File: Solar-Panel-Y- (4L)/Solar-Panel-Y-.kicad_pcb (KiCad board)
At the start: 4 copper layers, 64 x 58 mm, 85 parts, among them J1 FTS-107-01-X-DV-A, J2 BM02B-SRSS-TB, Q1 BSS138DWQ-7, Q2 MBT2222ADW1T1, Q3 BSS138DWQ-7, Q4 MBT2222ADW1T1, SW1 D2F-L2-A1, SW2 D2F-L2-A, U1 BQ25570RGRR, U2 TSL2561

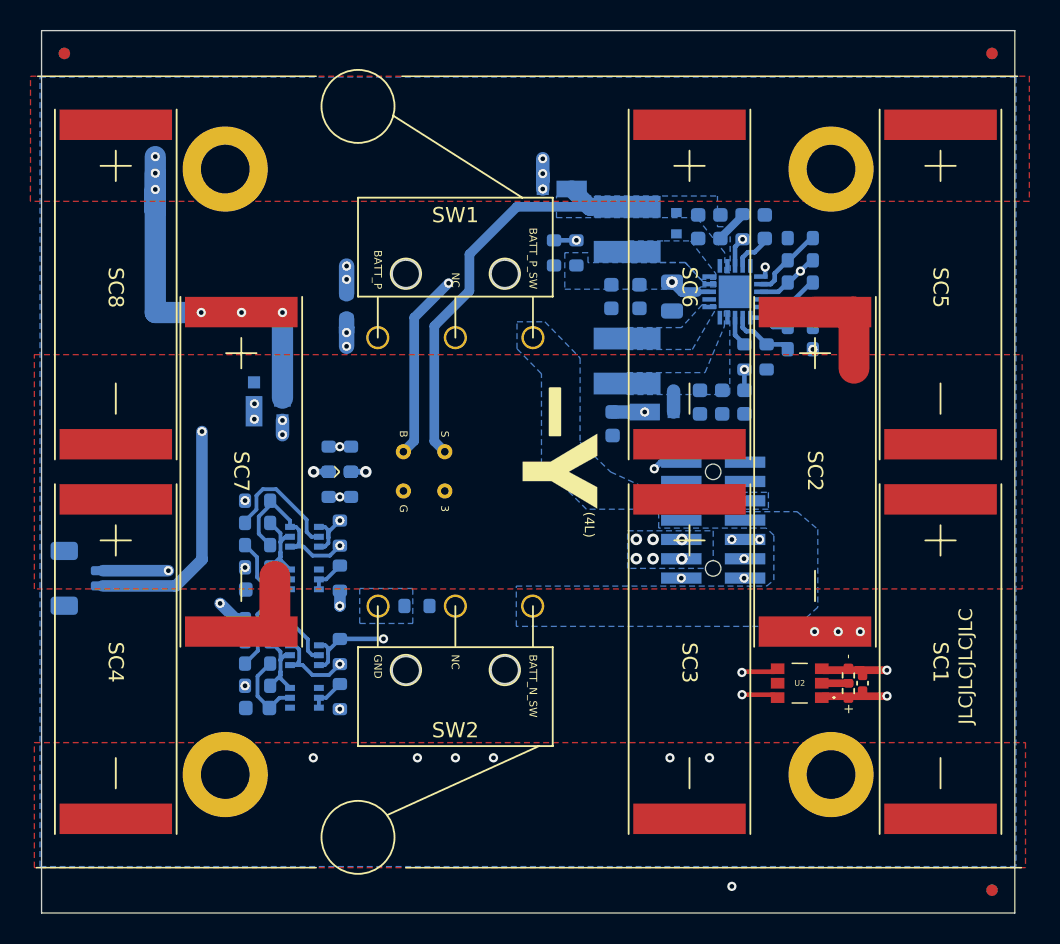
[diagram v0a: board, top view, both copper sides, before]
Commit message: Y- board changes for Rev B3/01
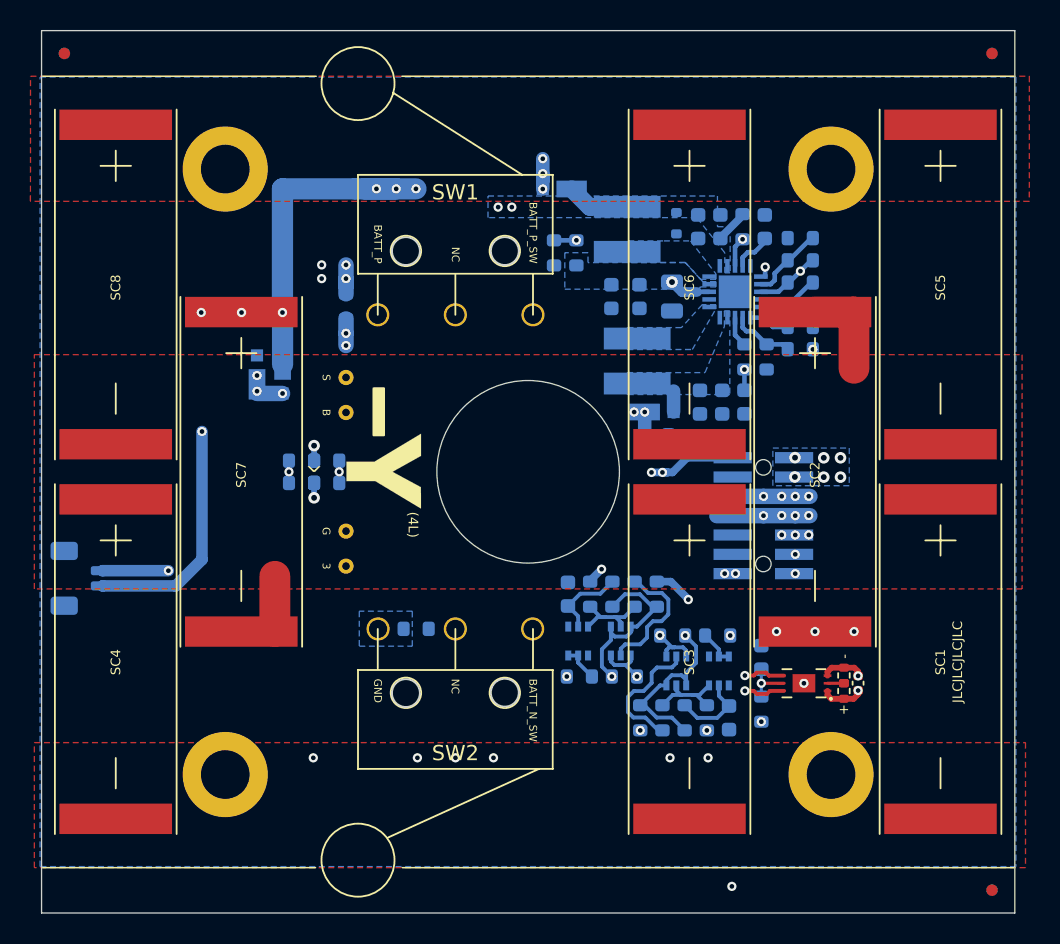
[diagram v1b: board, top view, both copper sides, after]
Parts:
- added C14: 1uF, Capacitor_SMD:C_0603_1608Metric, B.Cu at (120.3, 76.2)
- added R32: 1K, Resistor_SMD:R_0603_1608Metric, B.Cu at (120.3, 79.6)
- Q1, Q3: value BSS138DWQ-7 -> NX3008NBKS
- R1, R12, R13, R16, R17, R18, R2, R3, R31, R4: value 0 -> 0R
- R14, R15, R19, R20: value DNI -> DNI (0R)
- R21, R26: value 680 -> 680R
- U2: value TSL2561 -> BH1750FVI; footprint solarpanels:TSL2561 -> solarpanels:BH1750FVI
- moved C13 31.0 mm to (118.2, 80.2), turned to -90 degrees
- moved R28 29.6 mm to (116.7, 80.2), turned to 90 degrees
- moved R30 28.3 mm to (115.3, 80.2), turned to 90 degrees
- moved Q3 27.3 mm to (117.5, 77.1), turned to -90 degrees
- moved R26 27.1 mm to (113.8, 80.2), turned to 90 degrees
- moved R24 27.0 mm to (113.4, 72.0), turned to -90 degrees
- moved R29 26.0 mm to (112.3, 80.2), turned to 90 degrees
- moved R21 25.2 mm to (112.0, 72.0), turned to -90 degrees
- moved R27 25.2 mm to (117.4, 74.8), turned to 180 degrees
- moved Q4 24.5 mm to (114.7, 77.1), turned to -90 degrees
- moved R25 23.5 mm to (110.5, 72.0), turned to 90 degrees
- moved R23 21.9 mm to (109.0, 72.0), turned to -90 degrees
- moved R20 21.9 mm to (114.5, 74.8), turned to 180 degrees
- moved Q2 21.9 mm to (111.1, 75.1), turned to 90 degrees
- moved R19 20.9 mm to (111.3, 77.5), turned to 0 degrees
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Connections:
- J1 pad 1: unconnected-(J1-Pad1) -> BATT_P
- J1 pad 10: BATT_P -> GND
- J1 pad 12: BATT_P -> unconnected-(J1-Pin_12-Pad12)
- J1 pad 3: GND -> BATT_P
- J2 pad MP: (no net) -> GND
- U2 pad 4: SCL_LS -> SDA_LS
- U2 pad 5: unconnected-(U2-Pad5) -> Net-(U2-DVI)
- U2 pad 6: SDA_LS -> SCL_LS
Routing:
- net SCL_LS: track 49.6 -> 23.6 mm
- net SDA_LS: track 43.2 -> 20.4 mm
- net SDA: track 35.1 -> 16.4 mm
- net SCL: track 32.7 -> 19.6 mm
- net BATT_P_SW: track 41.6 -> 51.7 mm, vias 1 -> 5
- net VSOLAR: track 32.1 -> 24.5 mm, vias 0 -> 2
- net BATT_N_SW: track 30.6 -> 37.6 mm, vias 1 -> 5
- net COIL_N: track 26.6 -> 32.2 mm, vias 2 -> 3
- net COIL_P: track 32.4 -> 37.7 mm, vias 2 -> 3
- net /coil: track 7479.5 -> 7475.5 mm
- net Net-(U2-DVI): track 0.00 -> 3.30 mm, vias 0 -> 1
- net GND: track 4.56 -> 2.78 mm, vias 10 -> 11
- net /VSOLAR_FULL: track 30.6 -> 31.6 mm
- net +3V3: track 9.38 -> 8.62 mm, vias 10 -> 13
- net Net-(D3-K): track 10.8 -> 11.6 mm, vias 4 -> 3
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- added copper zone on In2.Cu, net BATT_N_SW
- added copper zone on In2.Cu, net BATT_P_SW
- removed copper zone on B.Cu, net BATT_N_SW
- removed copper zone on B.Cu, net BATT_P_SW
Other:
- outline, holes or cut-outs redrawn
- board text added: "1.BATT_P 3.BATT_P 5.BATT_P_SW 7.BATT_N_SW 9.3V3 11.SDA 13.SCL"
- board text added: "2.COIL_P 4.GND 6.BATT_P_SW 8.BATT_N_SW 10.GND 12.NC 14.COIL_N"
- board text added: "Rev B3/01"
- board text removed: "1.NC 3.GND 5.BATT_P_SW 7.BATT_N_SW 9.3V3 11.SDA 13.SCL"
- board text removed: "2.COIL_P 4.GND 6.BATT_P_SW 8.BATT_N_SW 10.BATT_P 12.BATT_P 14.COIL_N"
- board text removed: "Rev B2/01"

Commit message: Updated light sensor to OPT 3001, Updated solar diodes.
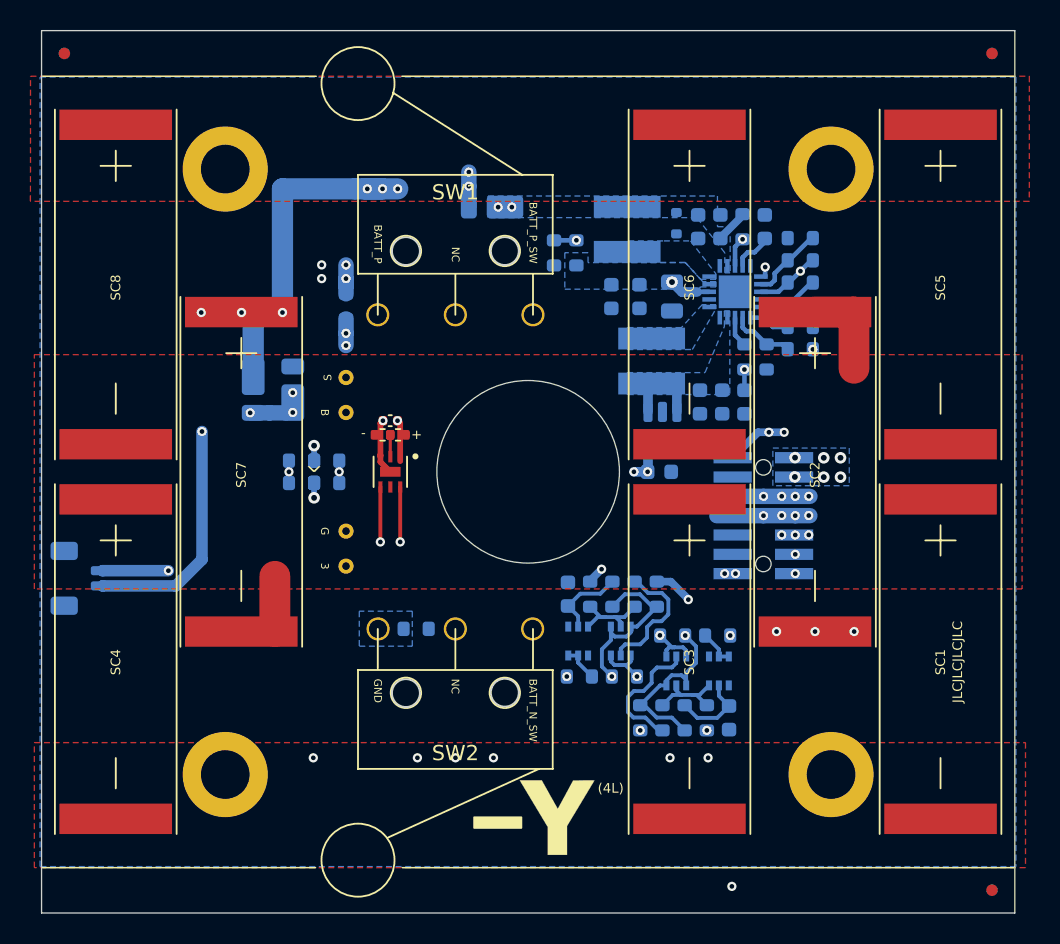
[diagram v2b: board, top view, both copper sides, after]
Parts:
- removed C14: 1uF, Capacitor_SMD:C_0603_1608Metric
- removed D5: MSS1P4-M3_89A, solarpanels:MICROSMP
- removed the R32 at (120.3, 79.6)
- added U3: MAX40200AUK, Package_TO_SOT_SMD:SOT-23-5, B.Cu at (113.8, 61.2)
- D2, D3, D4: value MSS1P4-M3_89A -> DFLS130L-7; footprint solarpanels:MICROSMP -> Diode_SMD:D_PowerDI-123
- U2: value BH1750FVI -> OPT3001; footprint solarpanels:BH1750FVI -> solarpanels:OPT3001
- moved C1 35.3 mm to (95.9, 60.6), turned to 0 degrees
- moved R2 34.2 mm to (95.4, 61.6), turned to 0 degrees
- moved R1 33.8 mm to (96.4, 61.6), turned to 0 degrees
- moved U2 30.5 mm to (95.9, 64.0), turned to -90 degrees
- moved Ref** 30.1 mm to (123.9, 87.7), turned to 0 degrees
- moved D2 17.2 mm to (102.6, 46.6), turned to 180 degrees
- moved D3 2.55 mm to (89.5, 58.6)
- moved C11 2.41 mm to (113.6, 64.0)
- moved D4 2.17 mm to (86.9, 58.6)
- moved L2 0.95 mm to (113.1, 56.7)
- renumbered R31 to R32, S to TP1, G to TP2, 3 to TP3, B to TP4
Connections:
- C10 pad 1: Net-(D2-A) -> Net-(U1-VOUT)
- C8 pad 1: Net-(D2-A) -> Net-(U1-VOUT)
- D2 pad 1: +3V3 -> VSOLAR
- D2 pad 2: Net-(D2-A) -> /VSOLAR_FULL
- L2 pad 2: Net-(D2-A) -> Net-(U1-VOUT)
- U1 pad 14: Net-(D2-A) -> Net-(U1-VOUT)
- U2 pad 4: SDA_LS -> SCL_LS
- U2 pad 5: Net-(U2-DVI) -> unconnected-(U2-INT-Pad5)
- U2 pad 6: SCL_LS -> SDA_LS
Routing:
- net SDA_LS: track 20.4 -> 40.8 mm
- net SCL_LS: track 23.6 -> 36.5 mm
- net COIL_P: track 37.7 -> 46.5 mm
- net VSOLAR: track 24.5 -> 20.5 mm
- net Net-(U1-VOUT): track 0.00 -> 3.49 mm
- net Net-(U2-DVI): track 3.30 -> 0.00 mm, vias 1 -> 0
- net /VSOLAR_FULL: track 31.6 -> 29.6 mm, vias 9 -> 8
- net Net-(D2-A): track 1.38 -> 0.00 mm
- net GND: track 2.78 -> 3.80 mm, vias 11 -> 10
- net Net-(D3-K): track 11.6 -> 12.4 mm
- net +3V3: track 8.62 -> 8.94 mm, vias 13 -> 12
- added copper zone on B.Cu, net Net-(U1-VOUT)
- removed copper zone on B.Cu, net Net-(D2-A)
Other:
- board text added: "3"
- board text added: "B"
- board text added: "G"
- board text added: "S"

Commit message: Updated Mounting Holes
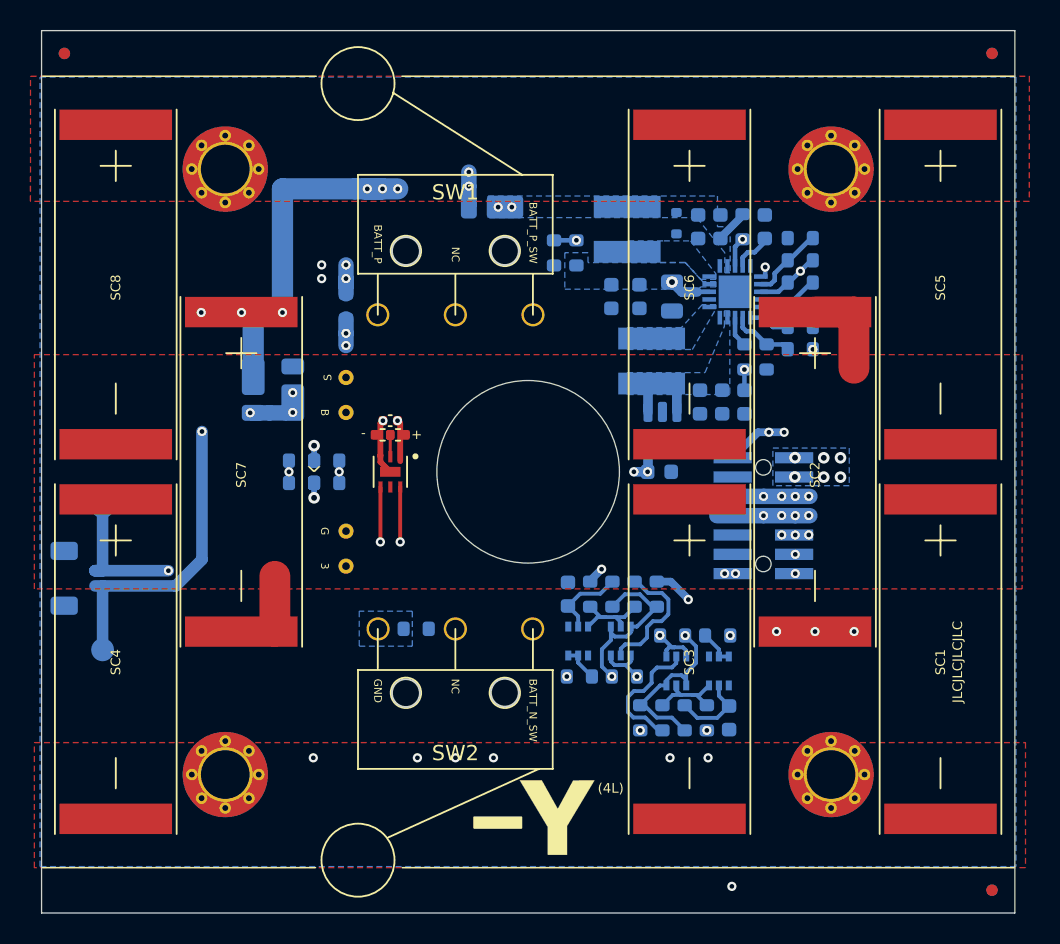
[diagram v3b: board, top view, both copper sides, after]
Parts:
- added TP5: TP, TestPoint:TestPoint_Pad_D1.5mm, B.Cu at (77.0, 66.3)
- added TP6: TP, TestPoint:TestPoint_Pad_D1.5mm, B.Cu at (77.0, 75.7)
- H1, H2, H3, H4: footprint MountingHole:MountingHole_3.2mm_M3_DIN965_Pad -> solarpanels:MountingHole_3.2mm_M3_DIN965_Pad_TopBottom
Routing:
- net BATT_N_SW: track 37.6 -> 42.8 mm
- net BATT_P_SW: track 51.7 -> 56.4 mm

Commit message: B3/02 Updates
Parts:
- C1: value 1uF -> 0.1uF
- REF** (x6): value Fiducial_0.75mm_Mask1.5mm -> Fiducial_1mm_Mask2mm; footprint Fiducial:Fiducial_0.75mm_Mask1.5mm -> Fiducial:Fiducial_1mm_Mask2mm
- moved D2 1.99 mm to (100.8, 45.7)
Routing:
- net /VSOLAR_FULL: track 29.6 -> 23.3 mm
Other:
- board text added: "Rev B3/02"
- board text removed: "Rev B3/01"

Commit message: Minor Fixes
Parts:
- renumbered R32 to R31
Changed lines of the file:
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@@
     (property "ki_keywords" "r resistor")
     (attr smd)
-    (fp_text reference "R32" (at 0 1.22) (layer "B.SilkS")
+    (fp_text reference "R31" (at 0 1.22) (layer "B.SilkS")
         (effects (font (size 0.508 0.508) (thickness 0.1016)) (justify mirror))
     )

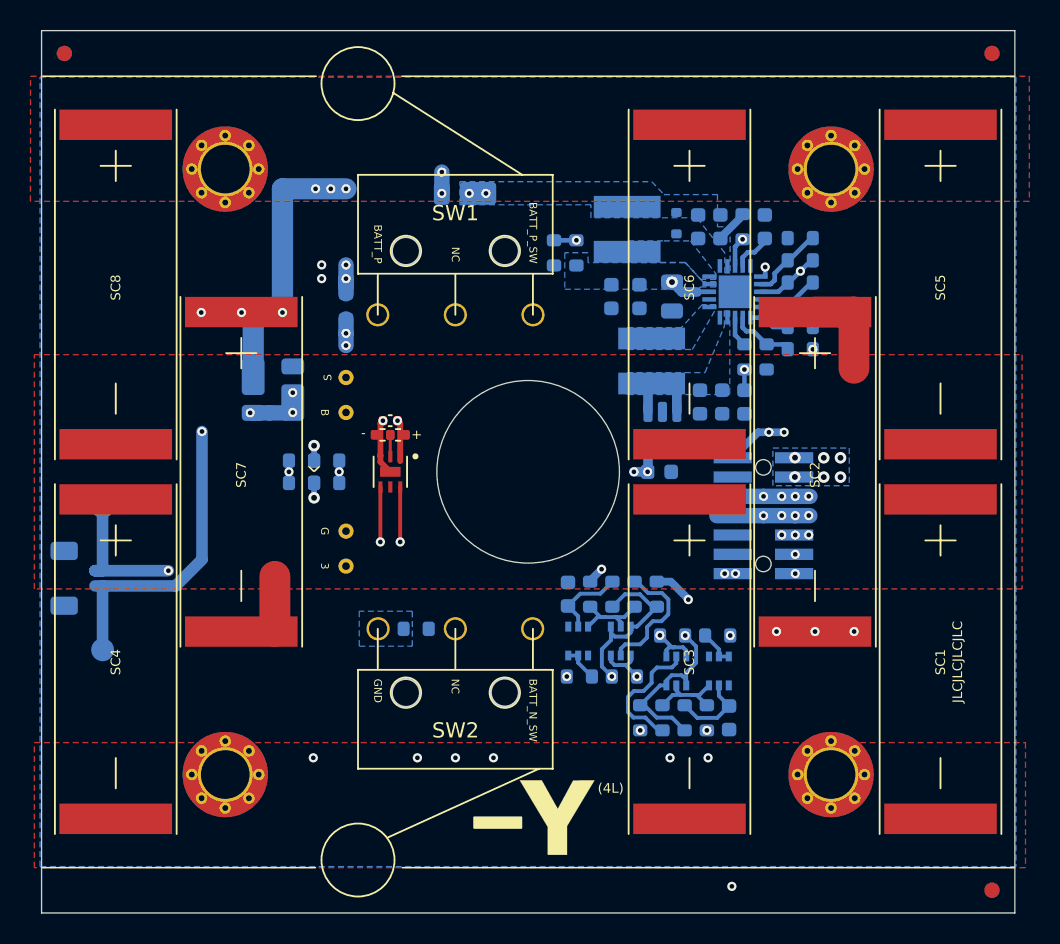
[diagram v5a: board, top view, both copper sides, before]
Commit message: Minor placement updates on -Y board
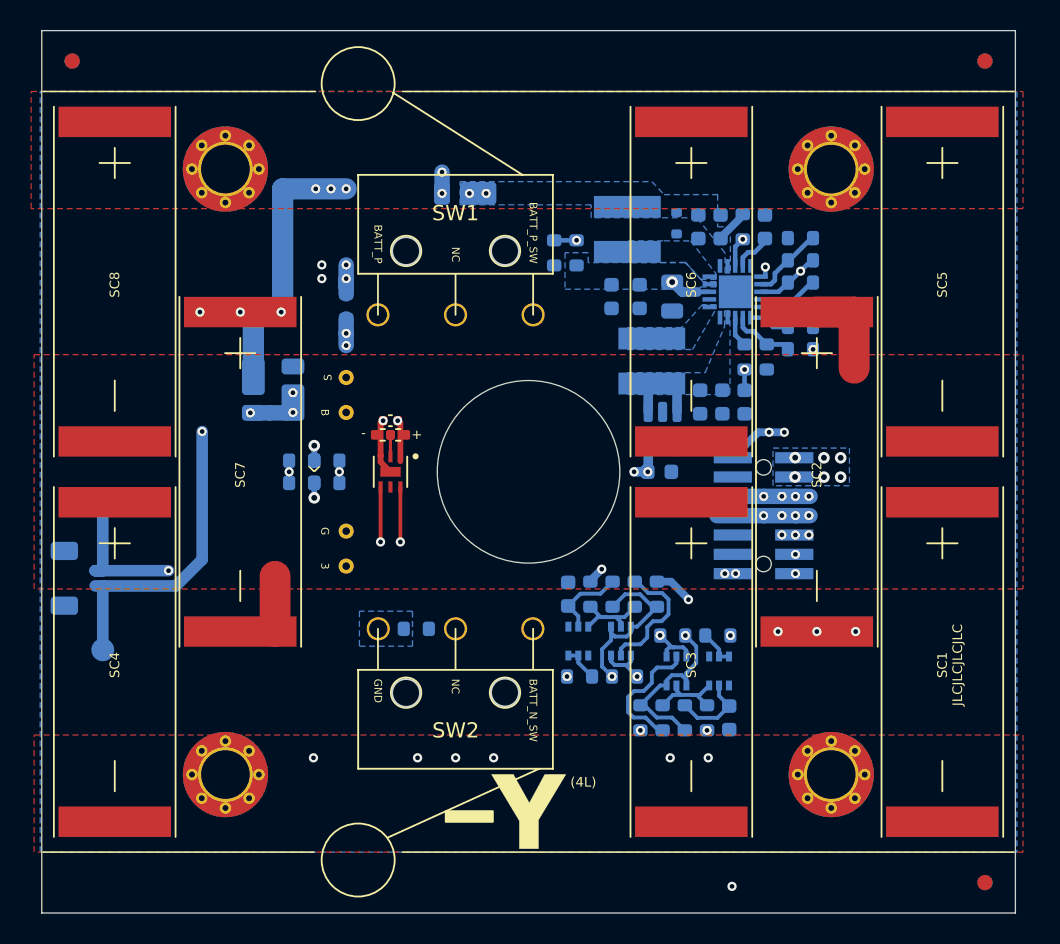
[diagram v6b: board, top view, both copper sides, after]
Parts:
- moved Ref** 1.91 mm to (122.1, 87.3)
- moved REF** 0.72 mm to (75.0, 37.0) (x2)
- moved REF** 0.68 mm to (135.0, 37.0) (x2)
- moved REF** 0.68 mm to (135.0, 91.0) (x2)
- moved SC1 0.23 mm to (132.2, 66.0)
- moved SC3 0.23 mm to (115.7, 66.0)
- moved SC5 0.22 mm to (132.2, 41.0)
- moved SC6 0.22 mm to (115.7, 41.0)
- moved SC4 0.20 mm to (77.8, 66.0)
- moved SC8 0.20 mm to (77.8, 41.0)
- moved SC2 0.12 mm to (124.0, 53.5)
- moved SC7 0.07 mm to (86.0, 53.5)

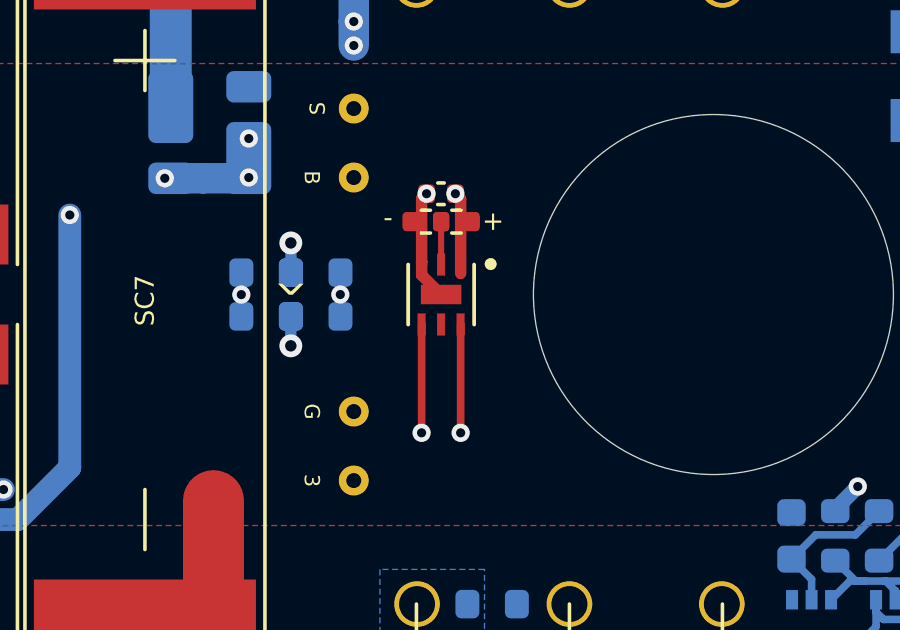
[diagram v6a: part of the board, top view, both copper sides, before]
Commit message: Updated Sun Sensor to OPT4001
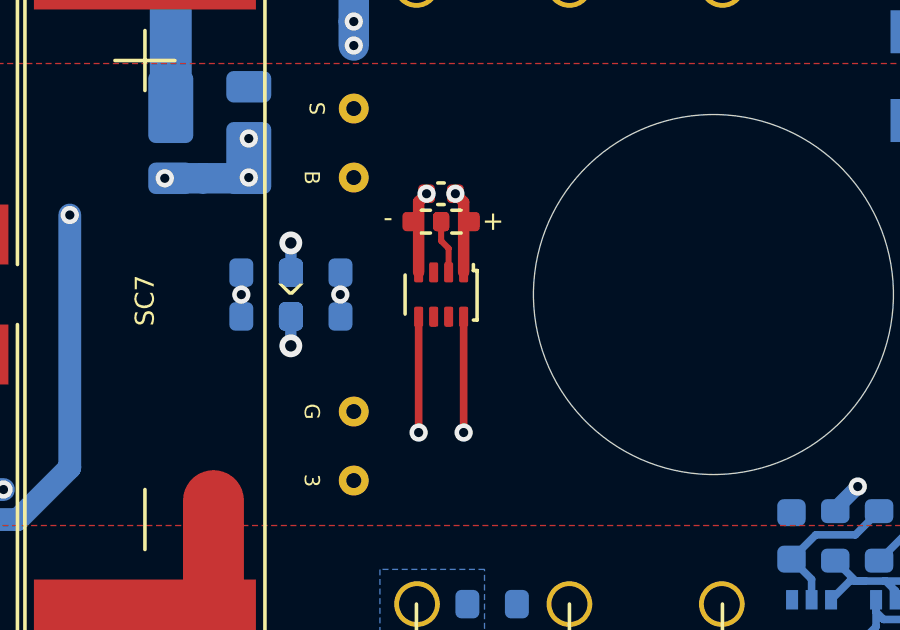
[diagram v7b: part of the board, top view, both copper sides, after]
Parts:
- U2: value OPT3001 -> OPT4001; footprint solarpanels:OPT3001 -> Package_TO_SOT_SMD:SOT-583-8
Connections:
- U2 pad 3: GND -> unconnected-(U2-NC-Pad3)
- U2 pad 4: SCL_LS -> GND
- U2 pad 5: unconnected-(U2-INT-Pad5) -> SCL_LS
- U2 pad 6: SDA_LS -> unconnected-(U2-NC-Pad6)
- U2 pad 7: GND -> unconnected-(U2-INT-Pad7)
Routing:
- net GND: track 3.80 -> 2.73 mm
